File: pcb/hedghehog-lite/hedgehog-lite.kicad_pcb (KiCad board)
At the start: 2 copper layers, 303.6 x 95 mm, 156 parts, among them J1 Conn_01x04, J2 AVR-ISP-6, K0 1u, K1 1u, K10 1u, K11 1u, K12 1u, K13 1u, K14 1u, K15 1u, K16 1u, K17 1u, K18 1.5u, K2 1u, K20 1u, K21 1u, K22 1u, K23 1u, K24 1u, K25 1u, K26 1u, K27 2.25u, K3 1u, K30 1u, K31 1u, K32 1u, K33 1u, K34 1u, K35 1u, K36 2.75u, K38 1u, K4 1u, K40 1u, K41 1.25u, K42 1.25u, K43 2.75u, K44 1u, K45 1u, K46 1u, K5 1u, K50 1u, K51 1u, K52 1u, K53 1u, K54 1u, K6 1u, K60 1u, K61 1u, K62 1u, K63 1u, K64 1u, K7 1u, K70 1u, K71 1u, K72 1u, K73 1u, K74 1u, K8 2u, K81 1u, K82 1u, K83 1u, K84 1u, K88 1u, SW1 Reset, SW2 SSSS811101, U1 ATmega32U4-M, Y1 16MHz

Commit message: Small PCB fixes and improvements
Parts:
- added TH1: jlcpcb_tooling, max_customs:jlcpcb_tooling, F.Cu at (52.0, 118.1)
- added TH2: jlcpcb_tooling, max_customs:jlcpcb_tooling, F.Cu at (349.9, 97.4)
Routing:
- net GND: track 801.3 -> 853.4 mm, vias 17 -> 21
- net LED_PWR_P: track 594.1 -> 635.6 mm, vias 6 -> 8

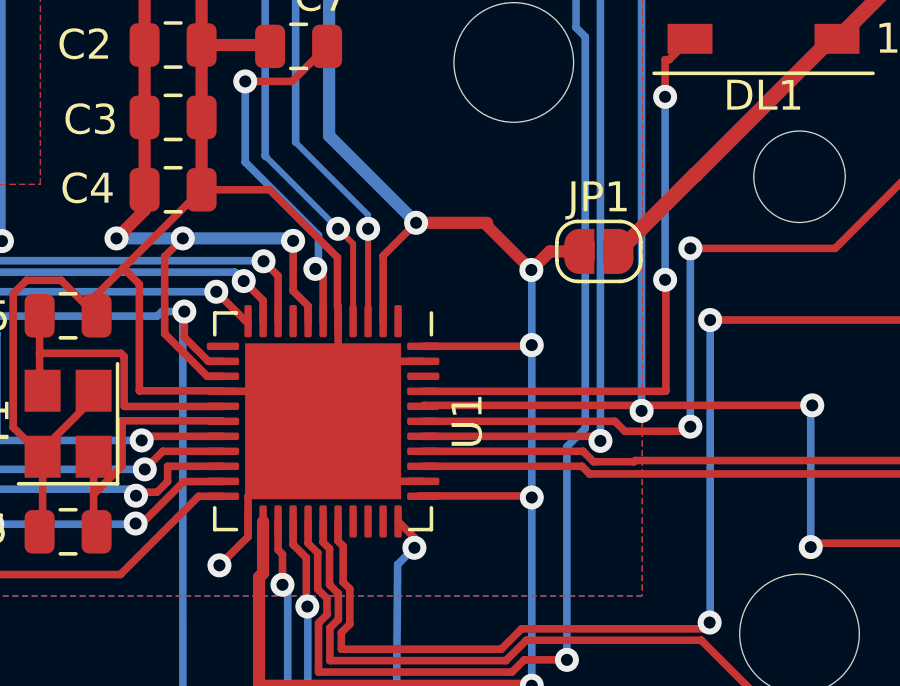
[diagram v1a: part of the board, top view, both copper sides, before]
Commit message: Improved GND connection for atmega
This should not be needed but now all pins are connected to an external track
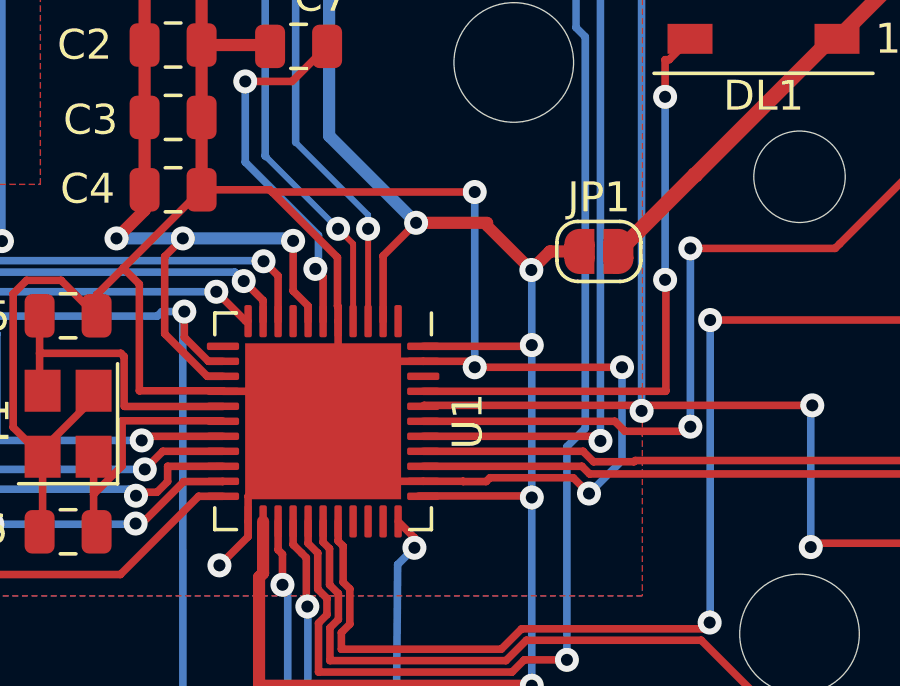
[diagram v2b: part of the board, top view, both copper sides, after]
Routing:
- net GND: track 853.4 -> 883.3 mm, vias 21 -> 25
